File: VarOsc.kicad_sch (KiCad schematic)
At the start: 18 parts, among them J1 Pitch_ANT, Q5 SMP5484, Q6 MMBT3906, Q7 MMBT3906

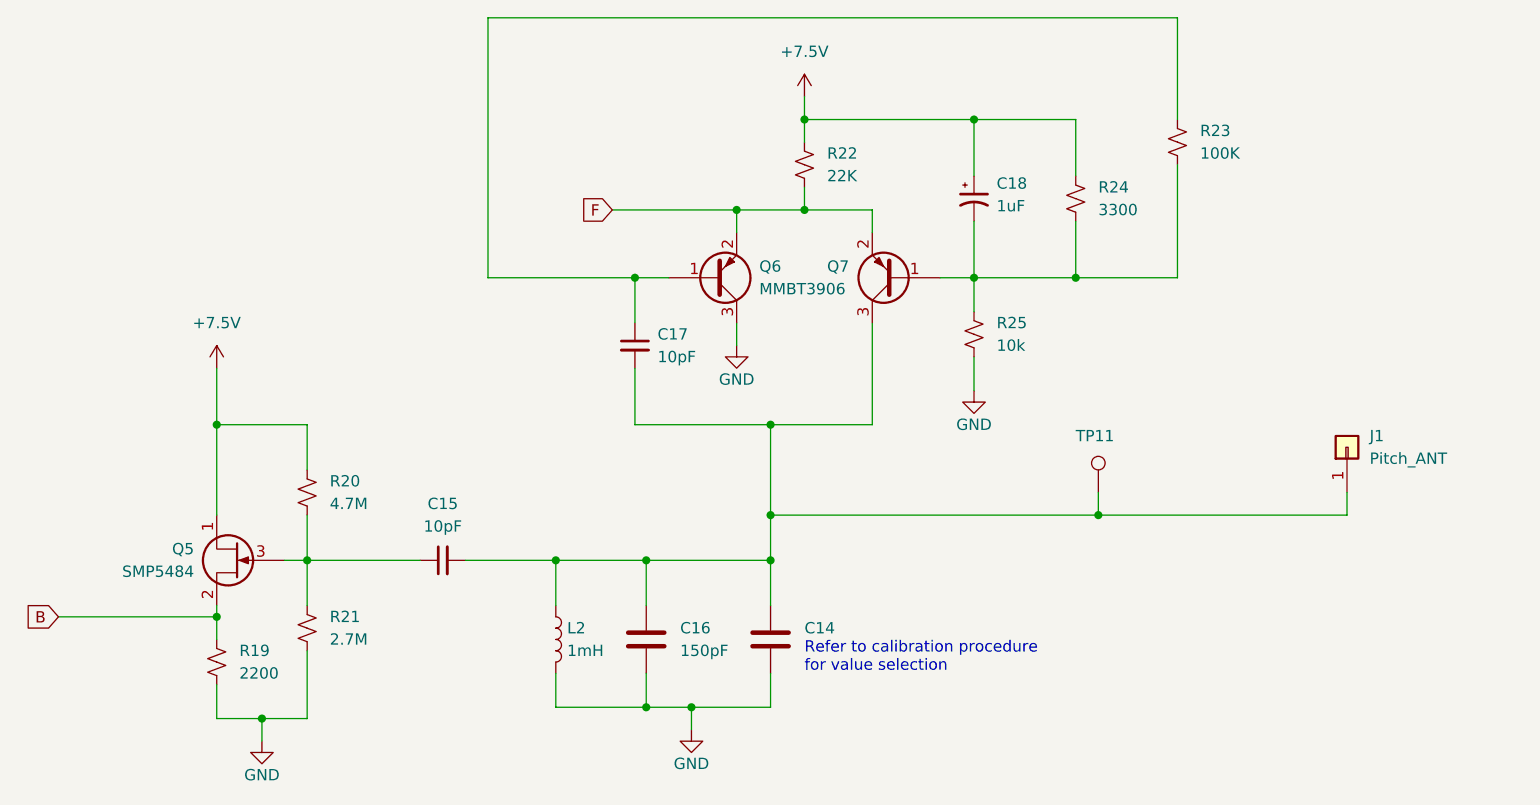
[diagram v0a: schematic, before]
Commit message: Components mostly placed
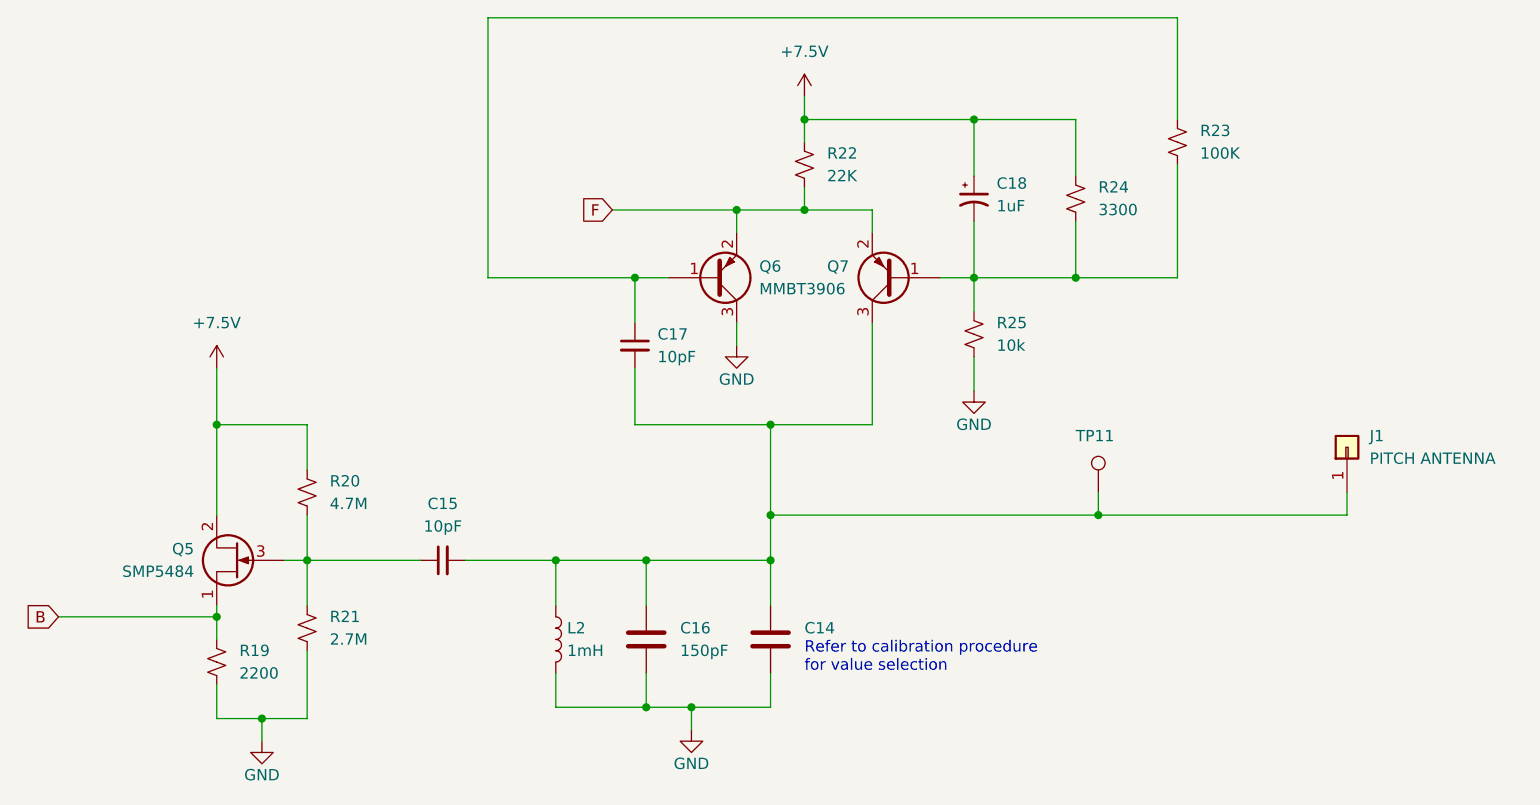
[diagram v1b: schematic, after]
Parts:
- C18: footprint Capacitor_Tantalum_SMD:CP_EIA-1608-08_AVX-J -> Capacitor_Tantalum_SMD:CP_EIA-2012-12_Kemet-R_Pad1.30x1.05mm_HandSolder
- J1: value Pitch_ANT -> PITCH ANTENNA; footprint MountingHole:MountingHole_3.2mm_M3_Pad_Via -> MountingHole:MountingHole_4.3mm_M4_Pad_Via
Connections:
- net +7.5V: now also Q5.2 (D); no longer Q5.1 (S)
- net B: now also Q5.1 (S); no longer Q5.2 (D)
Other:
- moved on the sheet: Q5
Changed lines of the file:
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@@
       (effects (font (size 1.27 1.27)) (justify left))
     )
-    (property "Footprint" "Capacitor_Tantalum_SMD:CP_EIA-1608-08_AVX-J" (id 2) (at 166.37 50.8 0)
+    (property "Footprint" "Capacitor_Tantalum_SMD:CP_EIA-2012-12_Kemet-R_Pad1.30x1.05mm_HandSolder" (id 2) (at 166.37 50.8 0)
       (effects (font (size 1.27 1.27)) hide)
     )
@@
       (effects (font (size 1.27 1.27)) (justify right))
     )
-    (property "Value" "Pitch_ANT" (id 1) (at 210.82 80.0099 90)
+    (property "Value" "PITCH ANTENNA" (id 1) (at 210.82 80.0099 90)
       (effects (font (size 1.27 1.27)) (justify right))
     )
-    (property "Footprint" "MountingHole:MountingHole_3.2mm_M3_Pad_Via" (id 2) (at 208.28 78.74 0)
+    (property "Footprint" "MountingHole:MountingHole_4.3mm_M4_Pad_Via" (id 2) (at 208.28 78.74 0)
       (effects (font (size 1.27 1.27)) hide)
     )
@@
     (pin "2")
   )
-  (symbol (lib_id "Device:Q_NJFET_SDG") (at 83.82 91.44 180) (unit 1)
+  (symbol (lib_id "Device:Q_NJFET_SDG") (at 83.82 91.44 0) (mirror y) (unit 1)
     (in_bom yes) (on_board yes) (fields_autoplaced)
     (property "Reference" "Q5" (id 0) (at 78.74 90.1699 0)
@@
       (effects (font (size 1.27 1.27)) (justify left))
     )
-    (property "Footprint" "Package_TO_SOT_SMD:SOT-23" (id 2) (at 78.74 93.98 0)
+    (property "Footprint" "Package_TO_SOT_SMD:SOT-23" (id 2) (at 78.74 88.9 0)
       (effects (font (size 1.27 1.27)) hide)
     )

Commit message: Better component placements
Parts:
- removed TP11: TestPoint, TestPoint:TestPoint_Pad_D1.0mm, symbol Connector:TestPoint
- added C14_TEST1: C, Capacitor_THT:C_Disc_D3.0mm_W1.6mm_P2.50mm, symbol Device:C
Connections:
- net GND: now also C14_TEST1.2
- net at C14.1, C15.2, C16.1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: now also C14_TEST1.1
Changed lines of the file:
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@@
   (junction (at 86.36 109.22) (diameter 0) (color 0 0 0 0)
   )
+  (junction (at 143.51 107.95) (diameter 0) (color 0 0 0 0)
+  )
   (junction (at 166.37 59.69) (diameter 0) (color 0 0 0 0)
   )
@@
   (junction (at 139.7 52.07) (diameter 0) (color 0 0 0 0)
   )
-  (junction (at 180.34 86.36) (diameter 0) (color 0 0 0 0)
-  )
   (junction (at 143.51 86.36) (diameter 0) (color 0 0 0 0)
   )
@@
     (stroke (width 0) (type default) (color 0 0 0 0))
   )
-  (wire (pts (xy 180.34 83.82) (xy 180.34 86.36))
-    (stroke (width 0) (type default) (color 0 0 0 0))
-  )
   (wire (pts (xy 189.23 30.48) (xy 111.76 30.48))
     (stroke (width 0) (type default) (color 0 0 0 0))
@@
     (stroke (width 0) (type default) (color 0 0 0 0))
   )
+  (wire (pts (xy 184.15 96.52) (xy 184.15 91.44))
+    (stroke (width 0) (type default) (color 0 0 0 0))
+  )
   (wire (pts (xy 189.23 41.91) (xy 189.23 30.48))
     (stroke (width 0) (type default) (color 0 0 0 0))
@@
     (stroke (width 0) (type default) (color 0 0 0 0))
   )
-  (wire (pts (xy 143.51 107.95) (xy 134.62 107.95))
-    (stroke (width 0) (type default) (color 0 0 0 0))
-  )
   (wire (pts (xy 166.37 41.91) (xy 147.32 41.91))
     (stroke (width 0) (type default) (color 0 0 0 0))
@@
     (stroke (width 0) (type default) (color 0 0 0 0))
   )
+  (wire (pts (xy 184.15 104.14) (xy 184.15 107.95))
+    (stroke (width 0) (type default) (color 0 0 0 0))
+  )
   (wire (pts (xy 134.62 107.95) (xy 134.62 110.49))
     (stroke (width 0) (type default) (color 0 0 0 0))
@@
     (stroke (width 0) (type default) (color 0 0 0 0))
   )
-  (wire (pts (xy 180.34 86.36) (xy 208.28 86.36))
+  (wire (pts (xy 143.51 86.36) (xy 208.28 86.36))
     (stroke (width 0) (type default) (color 0 0 0 0))
   )
@@
     (stroke (width 0) (type default) (color 0 0 0 0))
   )
+  (wire (pts (xy 134.62 107.95) (xy 143.51 107.95))
+    (stroke (width 0) (type default) (color 0 0 0 0))
+  )
   (wire (pts (xy 129.54 91.44) (xy 143.51 91.44))
     (stroke (width 0) (type default) (color 0 0 0 0))
@@
     (stroke (width 0) (type default) (color 0 0 0 0))
   )
-  (wire (pts (xy 143.51 86.36) (xy 180.34 86.36))
-    (stroke (width 0) (type default) (color 0 0 0 0))
-  )
   (wire (pts (xy 86.36 109.22) (xy 86.36 111.76))
     (stroke (width 0) (type default) (color 0 0 0 0))
   )
+  (wire (pts (xy 184.15 91.44) (xy 143.51 91.44))
+    (stroke (width 0) (type default) (color 0 0 0 0))
+  )
   (wire (pts (xy 111.76 59.69) (xy 128.27 59.69))
+    (stroke (width 0) (type default) (color 0 0 0 0))
+  )
+  (wire (pts (xy 143.51 107.95) (xy 184.15 107.95))
     (stroke (width 0) (type default) (color 0 0 0 0))
   )
@@
     (pin "2")
   )
-  (symbol (lib_id "Connector:TestPoint") (at 180.34 83.82 0) (unit 1)
-    (in_bom yes) (on_board yes)
-    (property "Reference" "TP11" (id 0) (at 177.8 77.47 0)
-      (effects (font (size 1.27 1.27)) (justify left))
-    )
-    (property "Value" "TestPoint" (id 1) (at 182.88 81.7879 0)
-      (effects (font (size 1.27 1.27)) (justify left) hide)
-    )
-    (property "Footprint" "TestPoint:TestPoint_Pad_D1.0mm" (id 2) (at 185.42 83.82 0)
-      (effects (font (size 1.27 1.27)) hide)
-    )
-    (property "Datasheet" "~" (id 3) (at 185.42 83.82 0)
-      (effects (font (size 1.27 1.27)) hide)
-    )
-    (pin "1")
-  )
   (symbol (lib_id "power:+7.5V") (at 81.28 69.85 0) (unit 1)
     (in_bom yes) (on_board yes) (fields_autoplaced)
@@
       (effects (font (size 1.27 1.27)) hide)
     )
+    (pin "1")
+    (pin "2")
+  )
+  (symbol (lib_id "Device:C") (at 184.15 100.33 0) (unit 1)
+    (in_bom yes) (on_board yes) (fields_autoplaced)
+    (property "Reference" "C14_TEST1" (id 0) (at 187.96 99.0599 0)
+      (effects (font (size 1.27 1.27)) (justify left))
+    )
+    (property "Value" "C" (id 1) (at 187.96 101.5999 0)
+      (effects (font (size 1.27 1.27)) (justify left))
+    )
+    (property "Footprint" "Capacitor_THT:C_Disc_D3.0mm_W1.6mm_P2.50mm" (id 2) (at 185.1152 104.14 0)
+      (effects (font (size 1.27 1.27)) hide)
+    )
+    (property "Datasheet" "~" (id 3) (at 184.15 100.33 0)
+      (effects (font (size 1.27 1.27)) hide)
+    )
